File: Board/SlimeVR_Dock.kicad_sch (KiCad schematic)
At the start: 30 parts, among them J1Fan1 Conn_01x04_Pin, J1Temp1 Conn_01x05_Pin, J1_Control1 Conn_01x03_Pin, J1_MainPW1 USB_C_Receptacle_USB2.0_16P, J1_Monitor1 Conn_01x03_Pin, J1_Prog1 Conn_01x03_Pin, Q1 AO3401A, Q6 BC817, U1 ESP32-C3-WROOM-02, U17 74HC165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

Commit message: pcb layout
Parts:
- Q1: value AO3401A -> NDT452AP; footprint Package_TO_SOT_SMD:SOT-23 -> Package_TO_SOT_SMD:SOT-223
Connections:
- net StepDown/Vin: now also Q1.2 (D), Q1.4 (D); no longer Q1.3 (D)
- net VBUS: now also Q1.3 (S); no longer Q1.2 (S)
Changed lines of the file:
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@@
 			)
 		)
-		(property "Value" "AO3401A"
+		(property "Value" "NDT452AP"
 			(at 86.36 102.616 0)
 			(effects
@@
 			)
 		)
-		(property "Footprint" "Package_TO_SOT_SMD:SOT-23"
+		(property "Footprint" "Package_TO_SOT_SMD:SOT-223"
 			(at 86.36 104.775 0)
 			(effects
@@
 		(pin "2"
 		)
+		(pin "4"
+		)
 		(instances

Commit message: upraveni veliskoti
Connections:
- no-connect marks 10 -> 12
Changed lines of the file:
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@@
+	)
+	(no_connect
+		(at 238.76 138.43)
 	)
 	(no_connect
@@
 	)
 	(no_connect
+		(at 254 138.43)
+	)
+	(no_connect

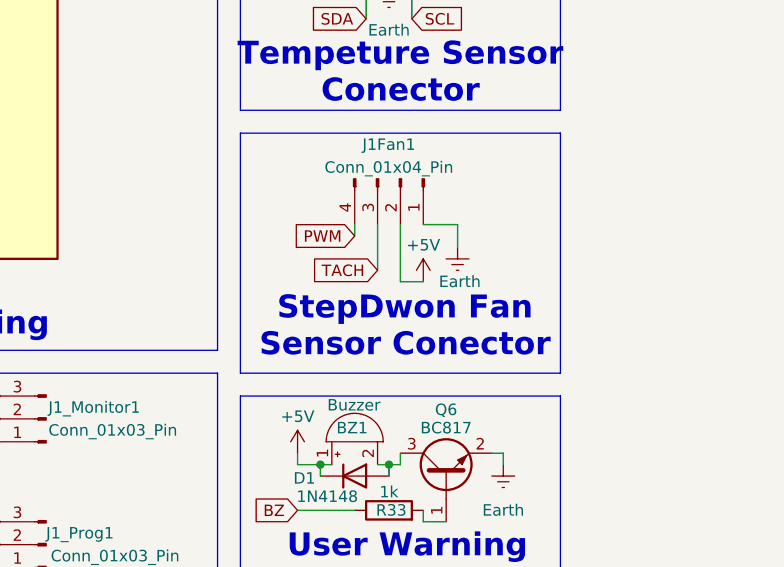
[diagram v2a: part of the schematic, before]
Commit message: Complete
-fixed tach pullup missing
- may have some unrecognised issues
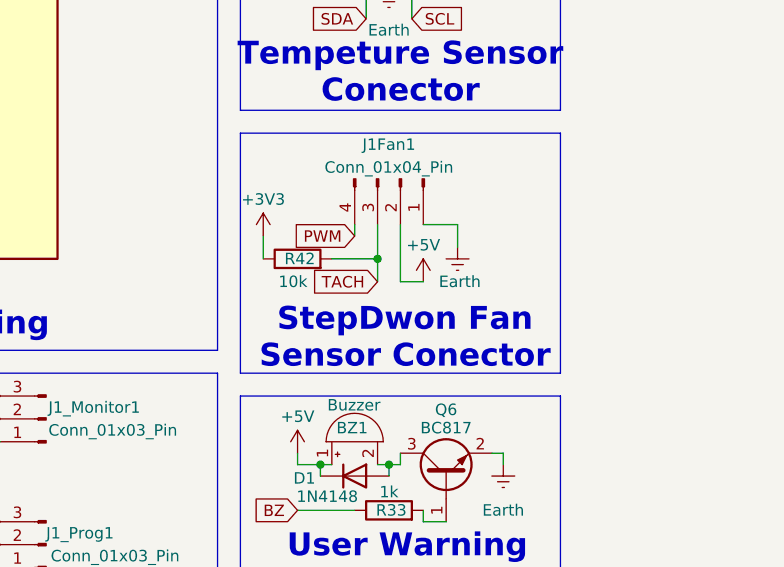
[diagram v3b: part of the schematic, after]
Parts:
- added R42: 10k, Resistor_SMD:R_0603_1608Metric, symbol Device:R
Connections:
- net +3V3: now also R42.1
- net TACH: now also R42.2
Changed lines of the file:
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@@
 	(text "StepDwon Fan \nSensor Conector"
 		(exclude_from_sim no)
-		(at 235.458 72.39 0)
+		(at 235.458 73.66 0)
 		(effects
 			(font
@@
 	)
 	(junction
+		(at 232.41 64.77)
+		(diameter 0)
+		(color 0 0 0 0)
+	)
+	(junction
 		(at 31.75 152.4)
 		(diameter 0)
@@
 	(wire
 		(pts
+			(xy 219.71 62.23) (xy 219.71 64.77)
+		)
+		(stroke
+			(width 0)
+			(type default)
+		)
+	)
+	(wire
+		(pts
 			(xy 154.94 151.13) (xy 154.94 149.86)
 		)
@@
 	(wire
 		(pts
-			(xy 232.41 66.04) (xy 232.41 60.96)
+			(xy 232.41 67.31) (xy 232.41 64.77)
 		)
 		(stroke
@@
 	(wire
 		(pts
+			(xy 227.33 64.77) (xy 232.41 64.77)
+		)
+		(stroke
+			(width 0)
+			(type default)
+		)
+	)
+	(wire
+		(pts
 			(xy 146.05 67.31) (xy 158.75 67.31)
 		)
@@
 	(wire
 		(pts
+			(xy 232.41 64.77) (xy 232.41 60.96)
+		)
+		(stroke
+			(width 0)
+			(type default)
+		)
+	)
+	(wire
+		(pts
 			(xy 196.85 151.13) (xy 196.85 149.86)
 		)
@@
 	(global_label "TACH"
 		(shape input)
-		(at 232.41 66.04 180)
+		(at 232.41 67.31 180)
 		(fields_autoplaced yes)
 		(effects
@@
 		)
 		(property "Intersheetrefs" "${INTERSHEET_REFS}"
-			(at 224.7681 66.04 0)
+			(at 224.7681 67.31 0)
 			(effects
 				(font
@@
 	(symbol
 		(lib_id "power:+3V3")
+		(at 219.71 62.23 0)
+		(unit 1)
+		(exclude_from_sim no)
+		(in_bom yes)
+		(on_board yes)
+		(dnp no)
+		(property "Reference" "#PWR027"
+			(at 219.71 66.04 0)
+			(effects
+				(font
+					(size 1.27 1.27)
+				)
+				(hide yes)
+			)
+		)
+		(property "Value" "+3V3"
+			(at 219.71 58.166 0)
+			(effects
+				(font
+					(size 1.27 1.27)
+				)
+			)
+		)
+		(property "Footprint" ""
+			(at 219.71 62.23 0)
+			(effects
+				(font
+					(size 1.27 1.27)
+				)
+				(hide yes)
+			)
+		)
+		(property "Datasheet" ""
+			(at 219.71 62.23 0)
+			(effects
+				(font
+					(size 1.27 1.27)
+				)
+				(hide yes)
+			)
+		)
+		(property "Description" "Power symbol creates a global label with name \"+3V3\""
+			(at 219.71 62.23 0)
+			(effects
+				(font
+					(size 1.27 1.27)
+				)
+				(hide yes)
+			)
+		)
+		(pin "1"
+		)
+		(instances
+			(project "SlimeVR_Dock"
+				(path "/06ff9557-1f9b-4670-8a34-bb7684a016dd"
+					(reference "#PWR027")
+					(unit 1)
+				)
+			)
+		)
+	)
+	(symbol
+		(lib_id "power:+3V3")
 		(at 118.11 46.99 0)
 		(unit 1)
@@
 					(unit 1)
 				)
+			)
+		)
+	)
+	(symbol
+		(lib_id "Device:R")
+		(at 223.52 64.77 90)
+		(unit 1)
+		(exclude_from_sim no)
+		(in_bom yes)
+		(on_board yes)
+		(dnp no)
+		(property "Reference" "R42"
+			(at 223.774 64.77 90)
+			(effects
+				(font
+					(size 1.27 1.27)
+				)
+			)
+		)
+		(property "Value" "10k"
+			(at 223.012 67.31 90)
+			(effects
+				(font
+					(size 1.27 1.27)
+				)
+			)
+		)
+		(property "Footprint" "Resistor_SMD:R_0603_1608Metric"
+			(at 223.52 66.548 90)
+			(effects
+				(font
+					(size 1.27 1.27)
+				)
+				(hide yes)
+			)
+		)
+		(property "Datasheet" "~"
+			(at 223.52 64.77 0)
+			(effects
+				(font
+					(size 1.27 1.27)
+				)
+				(hide yes)
+			)
+		)
+		(property "Description" "Resistor"
+			(at 223.52 64.77 0)
+			(effects
+				(font
+					(size 1.27 1.27)
+				)
+				(hide yes)
+			)
+		)
+		(pin "2"
+		)
+		(pin "1"
+		)
+		(instances
+			(project "SlimeVR_Dock"
+				(path "/06ff9557-1f9b-4670-8a34-bb7684a016dd"
+					(reference "R42")
+					(unit 1)
+				)

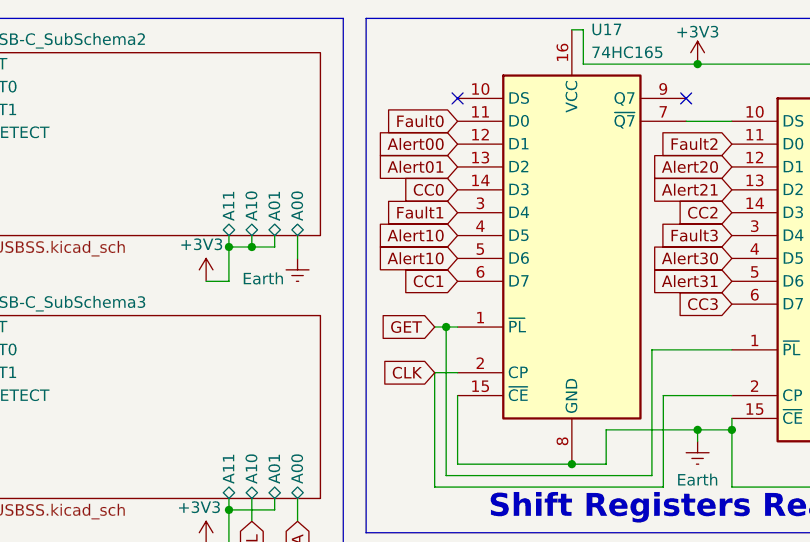
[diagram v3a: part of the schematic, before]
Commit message: fixed chema, finished silkscreen
-Alert10 was duplicated
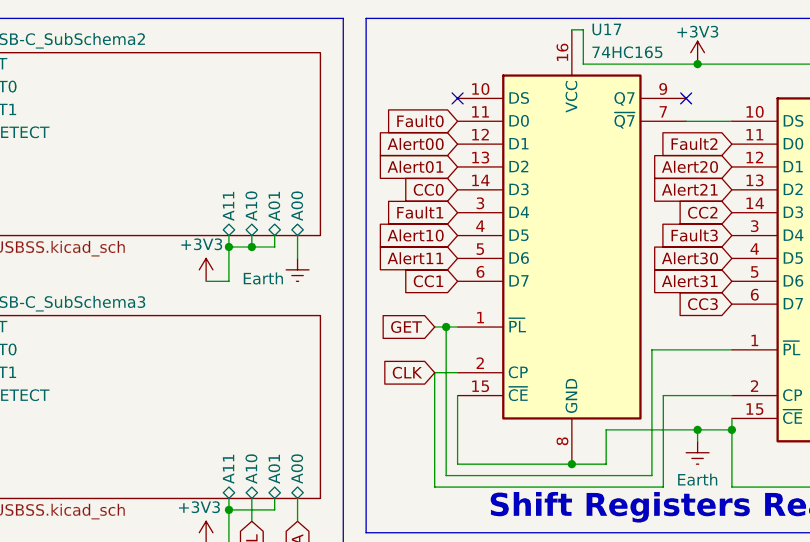
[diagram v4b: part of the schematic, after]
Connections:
- net Alert10: no longer U17.5 (D6)
- net Alert11: now also U17.5 (D6)
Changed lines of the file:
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@@
+		)
+	)
+	(global_label "Alert11"
+		(shape input)
+		(at 146.05 44.45 180)
+		(fields_autoplaced yes)
+		(effects
+			(font
+				(size 1.27 1.27)
+			)
+			(justify right)
+		)
+		(property "Intersheetrefs" "${INTERSHEET_REFS}"
+			(at 136.2915 44.45 0)
+			(effects
+				(font
+					(size 1.27 1.27)
+				)
+				(justify right)
+				(hide yes)
+			)
 		)
 	)
@@
 			(effects
 				(font
-					(size 1.27 1.27)
-				)
-				(justify right)
-				(hide yes)
-			)
-		)
-	)
-	(global_label "Alert10"
-		(shape input)
-		(at 146.05 44.45 180)
-		(fields_autoplaced yes)
-		(effects
-			(font
-				(size 1.27 1.27)
-			)
-			(justify right)
-		)
-		(property "Intersheetrefs" "${INTERSHEET_REFS}"
-			(at 136.2915 44.45 0)
-			(effects
-				(font

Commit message: Updated fields for LCSC
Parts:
- J1_MainPW1: LCSC (none) -> C5178539
- Q1: LCSC (none) -> C274614
- Q6: LCSC (none) -> C39828
- U1: LCSC (none) -> C2934560
- U17, U18: LCSC (none) -> C5613
- U19: LCSC (none) -> C5947
- U2: LCSC (none) -> C970725
- U3: LCSC (none) -> C86534
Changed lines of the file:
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@@
 			)
 		)
+		(property "LCSC" "C5178539"
+			(at 35.56 129.54 0)
+			(effects
+				(font
+					(size 1.27 1.27)
+				)
+				(hide yes)
+			)
+		)
 		(pin "A8"
 		)
@@
 			)
 		)
+		(property "LCSC" "C39828"
+			(at 240.03 88.9 90)
+			(effects
+				(font
+					(size 1.27 1.27)
+				)
+				(hide yes)
+			)
+		)
 		(pin "2"
 		)
@@
 			)
 		)
+		(property "LCSC" "C2934560"
+			(at 246.38 123.19 90)
+			(effects
+				(font
+					(size 1.27 1.27)
+				)
+				(hide yes)
+			)
+		)
 		(pin "10"
 		)
@@
 			)
 		)
+		(property "LCSC" "C970725"
+			(at 81.28 129.54 90)
+			(effects
+				(font
+					(size 1.27 1.27)
+				)
+				(hide yes)
+			)
+		)
 		(pin "8"
 		)
@@
 			)
 		)
+		(property "LCSC" "C5613"
+			(at 189.23 44.45 0)
+			(effects
+				(font
+					(size 1.27 1.27)
+				)
+				(hide yes)
+			)
+		)
 		(pin "12"
 		)
@@
 			)
 		)
+		(property "LCSC" "C86534"
+			(at 177.8 140.97 0)
+			(effects
+				(font
+					(size 1.27 1.27)
+				)
+				(hide yes)
+			)
+		)
 		(pin "5"
 		)
@@
 			)
 		)
+		(property "LCSC" "C5613"
+			(at 158.75 41.91 0)
+			(effects
+				(font
+					(size 1.27 1.27)
+				)
+				(hide yes)
+			)
+		)
 		(pin "12"
 		)
@@
 			)
 		)
+		(property "LCSC" "C274614"
+			(at 81.28 102.87 0)
+			(effects
+				(font
+					(size 1.27 1.27)
+				)
+				(hide yes)
+			)
+		)
 		(pin "1"
 		)
@@
 			(at 157.48 99.06 0)
 			(effects
+				(font
+					(size 1.27 1.27)
+				)
+				(hide yes)
+			)
+		)
+		(property "LCSC" "C5947"
+			(at 157.48 99.06 0)
+			(effects

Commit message: new pdf schema
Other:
- company: (none) -> Skaut0071
- title: (none) -> SlimeVR Dock
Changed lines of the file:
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@@
 	(generator_version "9.0")
 	(paper "A4")
+	(title_block
+		(title "SlimeVR Dock")
+		(date "2026-04-10")
+		(rev "1.0")
+		(company "Skaut0071")
+	)
 	(text "User Warning"
 		(exclude_from_sim no)

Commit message: Total Power Suply layout overhall
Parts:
- J1Temp1: footprint Connector_PinHeader_2.54mm:PinHeader_1x05_P2.54mm_Vertical -> Connector_PinHeader_2.54mm:PinHeader_1x04_P2.54mm_Vertical

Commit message: New Power
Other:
- note added: "3V3 Power Regulator"
- note added: "StepDown Fan Sensor Conector"
- note added: "Tempature Sensor Conector"
- note added: "USB-C Connections"
- note removed: "3V3 Power Generator"
- note removed: "StepDwon Fan Sensor Conector"
- note removed: "Tempeture Sensor Conector"
- note removed: "USB-C Conections"
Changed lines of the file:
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@@
 		)
 	)
-	(text "Tempeture Sensor\nConector"
+	(text "Tempature Sensor\nConector"
 		(exclude_from_sim no)
 		(at 234.95 44.196 0)
@@
 		)
 	)
-	(text "3V3 Power Generator"
+	(text "3V3 Power Regulator"
 		(exclude_from_sim no)
 		(at 177.546 159.512 0)
@@
 		)
 	)
-	(text "USB-C Conections\n"
+	(text "USB-C Connections\n"
 		(exclude_from_sim no)
 		(at 76.2 88.138 0)
@@
 		)
 	)
-	(text "StepDwon Fan \nSensor Conector"
+	(text "StepDown Fan \nSensor Conector"
 		(exclude_from_sim no)
 		(at 235.458 73.66 0)
@@
 		)
 	)
-	(global_label "5VStepDwon"
+	(global_label "5VStepDown"
 		(shape input)
 		(at 71.12 77.47 180)
@@
 		)
 	)
-	(global_label "5VStepDwon"
+	(global_label "Data_Out"
 		(shape input)
-		(at 115.57 97.79 0)
+		(at 201.93 29.21 0)
 		(fields_autoplaced yes)
 		(effects
@@
 		)
 		(property "Intersheetrefs" "${INTERSHEET_REFS}"
-			(at 129.9246 97.79 0)
+			(at 213.3817 29.21 0)
 			(hide yes)
 			(show_name no)
@@
 		)
 	)
-	(global_label "Data_Out"
+	(global_label "Fault3"
 		(shape input)
-		(at 201.93 29.21 0)
+		(at 88.9 52.07 180)
 		(fields_autoplaced yes)
 		(effects
@@
 				(size 1.27 1.27)
 			)
-			(justify left)
+			(justify right)
 		)
 		(property "Intersheetrefs" "${INTERSHEET_REFS}"
-			(at 213.3817 29.21 0)
+			(at 79.9278 52.07 0)
 			(hide yes)
 			(show_name no)
@@
 					(size 1.27 1.27)
 				)
-				(justify left)
+				(justify right)
 			)
 		)
 	)
-	(global_label "Fault3"
+	(global_label "5VStepDown"
 		(shape input)
-		(at 88.9 52.07 180)
+		(at 115.57 97.79 0)
 		(fields_autoplaced yes)
 		(effects
@@
 				(size 1.27 1.27)
 			)
-			(justify right)
+			(justify left)
 		)
 		(property "Intersheetrefs" "${INTERSHEET_REFS}"
-			(at 79.9278 52.07 0)
+			(at 129.9246 97.79 0)
 			(hide yes)
 			(show_name no)
@@
 					(size 1.27 1.27)
 				)
-				(justify right)
+				(justify left)
 			)
 		)
